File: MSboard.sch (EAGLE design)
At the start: 30 parts, among them U1 MSP430F5342_RGZ_48

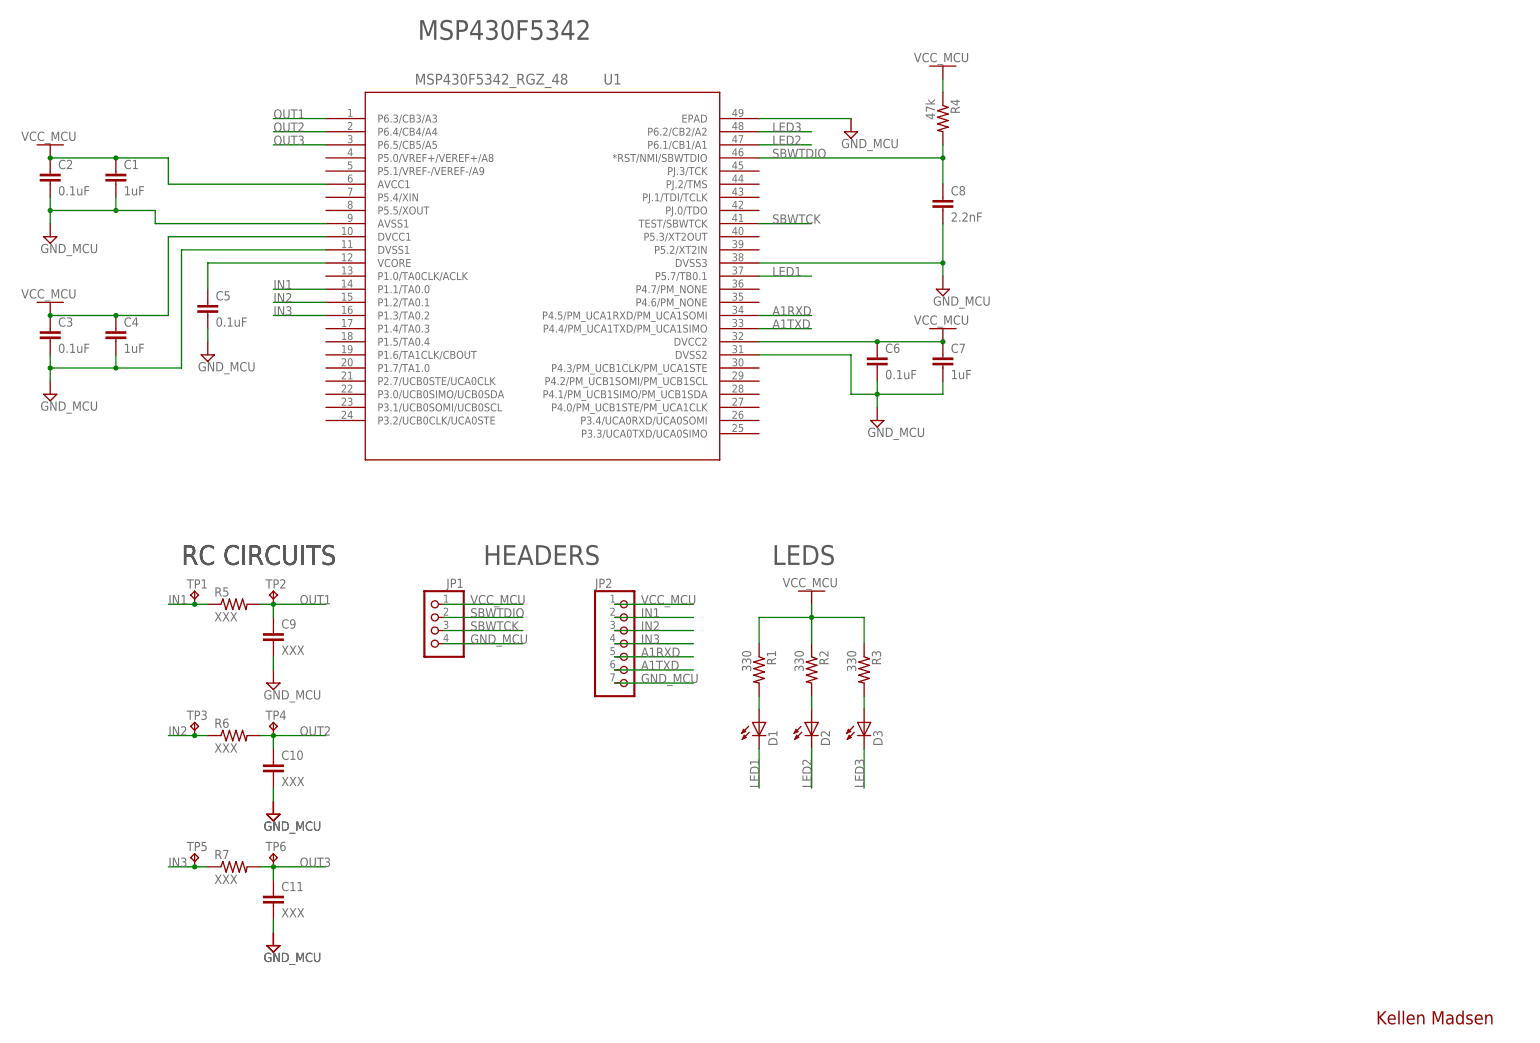
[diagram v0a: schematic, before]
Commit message: Updated Schematic and PCB
Ground Plane was poured, nets changed to VCC and GND, Errors Reduced.
Need to Run DRC and add top Polygon Pour.
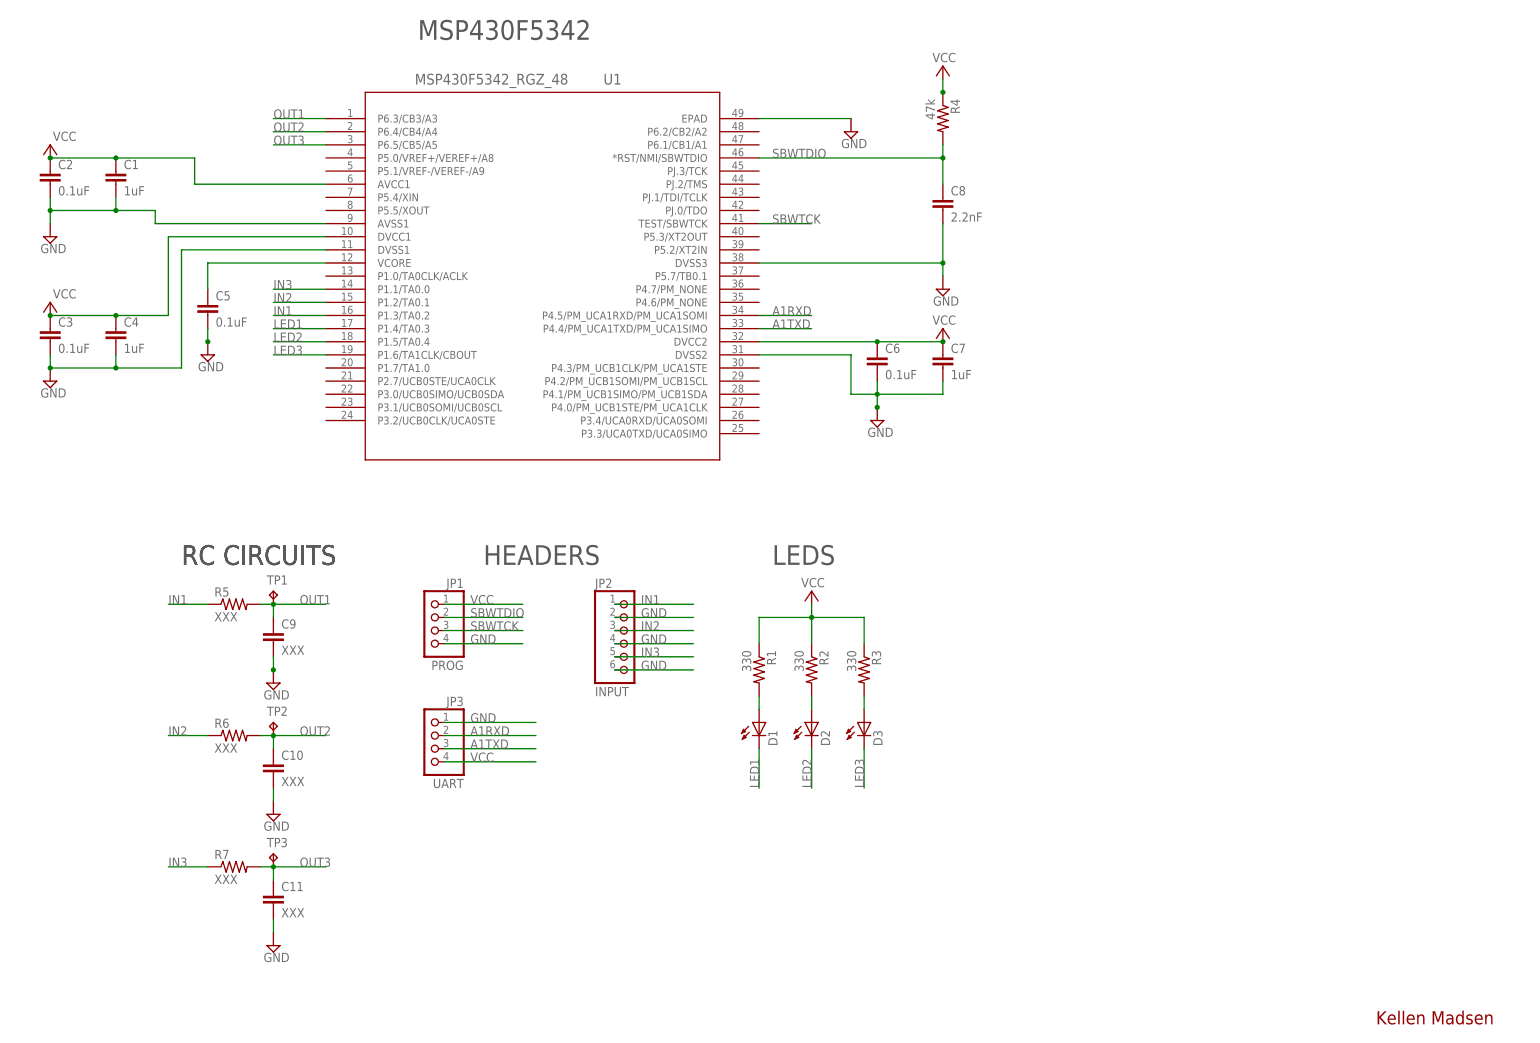
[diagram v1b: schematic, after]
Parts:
- removed TP4, TP5, TP6: TPPAD1-13Y, testpad:TPPAD1-13Y
- added JP3: UART, pinhead:PINHD-1X4
- JP1: value (none) -> PROG
- JP2: value (none) -> INPUT; device pinhead:PINHD-1X7 -> pinhead:PINHD-1X6
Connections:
- net N$3 renamed VCORE
- removed net GND_MCU: C3.2, C4.2, C6.2, C7.2, JP1.4, JP2.7, U1.DVSS1, U1.DVSS2
- removed net VCC_MCU: JP1.1, JP2.1
- net A1RXD: now also JP3.2; no longer JP2.5
- net A1TXD: now also JP3.3; no longer JP2.6
- net GND: now also C3.2, C4.2, C6.2, C7.2, JP1.4, JP2.2, JP2.4, JP2.6, JP3.1, U1.DVSS1, U1.DVSS2
- net IN1: now also JP2.1, U1.P1.3/TA0.2; no longer JP2.2, TP1.TP, U1.P1.1/TA0.0
- net IN2: no longer TP3.TP
- net IN3: now also JP2.5, U1.P1.1/TA0.0; no longer JP2.4, TP5.TP, U1.P1.3/TA0.2
- net LED1: now also U1.P1.4/TA0.3; no longer U1.P5.7/TB0.1
- net LED2: now also U1.P1.5/TA0.4; no longer U1.P6.1/CB1/A1
- net LED3: now also U1.P1.6/TA1CLK/CBOUT; no longer U1.P6.2/CB2/A2
- net OUT1: now also TP1.TP; no longer TP2.TP
- net OUT2: now also TP2.TP; no longer TP4.TP
- net OUT3: now also TP3.TP; no longer TP6.TP
- net VCC: now also JP1.1, JP3.4
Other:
- moved on the sheet: TP1, TP2, TP3
